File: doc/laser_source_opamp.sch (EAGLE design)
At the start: 12 parts, among them IC1 LM358N

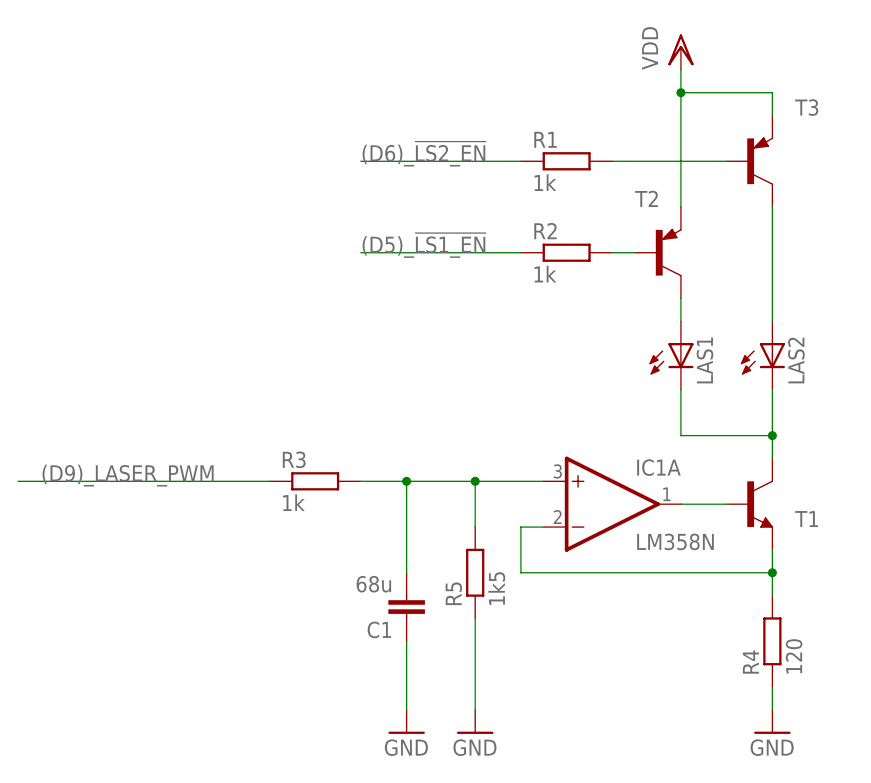
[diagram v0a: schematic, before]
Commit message: Laser power source schematics updated and tested @5V.
The previous version of schematics doesn't work as intended
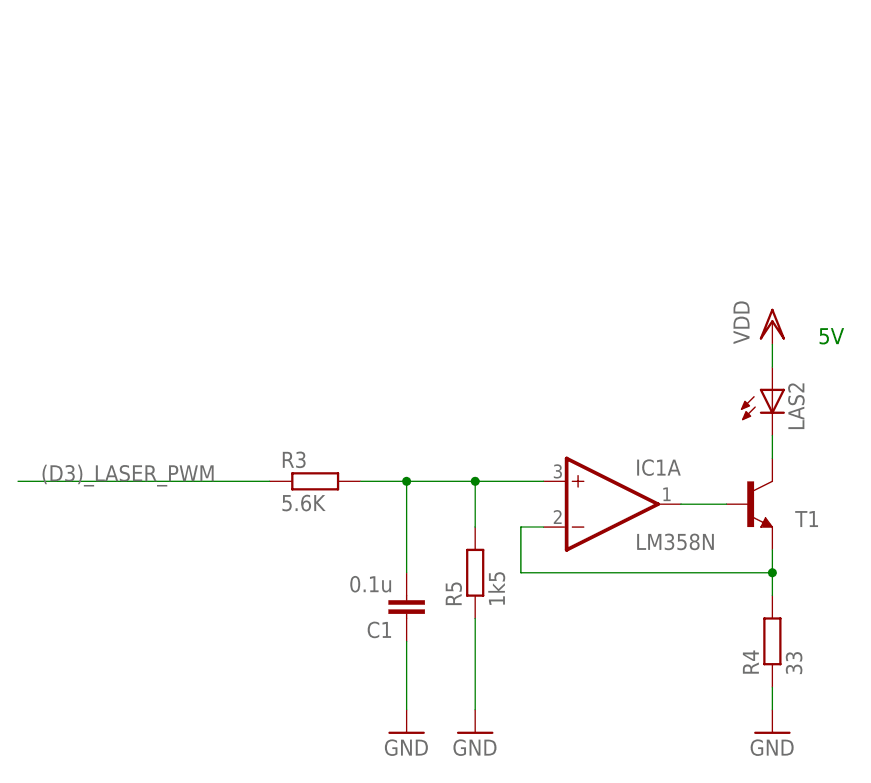
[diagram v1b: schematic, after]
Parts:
- removed LAS1: (no value), led:LED
- removed R1, R2: 1k, rcl:R-EU_0204/5
- removed T2, T3: (no value), transistor:-PNP-SOT23-EBC
- C1: value 68u -> 0.1u
- R3: value 1k -> 5.6K
- R4: value 120 -> 33
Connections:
- net (D9)_LASER_PWM renamed (D3)_LASER_PWM
- removed net (D5)_!LS1_EN!: R2.1
- removed net (D6)_!LS2_EN!: R1.1
- removed net N$10: R2.2, T2.B
- removed net N$7: R1.2, T3.B
- removed net N$8: LAS2.A, T3.C
- removed net N$9: LAS1.A, T2.C
- net N$4: no longer LAS1.C
- net VDD: now also LAS2.A; no longer T2.E, T3.E
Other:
- note added: "5V"
- moved on the sheet: LAS2
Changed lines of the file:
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@@
 </classes>
 <parts>
-<part name="R1" library="rcl" deviceset="R-EU_" device="0204/5" value="1k"/>
-<part name="R2" library="rcl" deviceset="R-EU_" device="0204/5" value="1k"/>
-<part name="R3" library="rcl" deviceset="R-EU_" device="0204/5" value="1k"/>
-<part name="R4" library="rcl" deviceset="R-EU_" device="0204/5" value="120"/>
-<part name="C1" library="capacitor-wima" deviceset="C" device="5/3.5" value="68u"/>
+<part name="R3" library="rcl" deviceset="R-EU_" device="0204/5" value="5.6K"/>
+<part name="R4" library="rcl" deviceset="R-EU_" device="0204/5" value="33"/>
+<part name="C1" library="capacitor-wima" deviceset="C" device="5/3.5" value="0.1u"/>
 <part name="GND1" library="supply1" deviceset="GND" device=""/>
 <part name="VDD1" library="supply1" deviceset="VDD" device=""/>
 <part name="T1" library="transistor" deviceset="*-NPN-" device="SOT89-BCE"/>
-<part name="T2" library="transistor" deviceset="*-PNP-" device="SOT23-EBC"/>
-<part name="T3" library="transistor" deviceset="*-PNP-" device="SOT23-EBC"/>
 <part name="GND2" library="supply1" deviceset="GND" device=""/>
 <part name="LAS2" library="led" deviceset="LED" device=""/>
-<part name="LAS1" library="led" deviceset="LED" device=""/>
 <part name="IC1" library="linear" deviceset="LM358" device="N"/>
 <part name="R5" library="rcl" deviceset="R-EU_" device="0204/5" value="1k5"/>
@@
 <sheet>
 <plain>
+<text x="76.2" y="53.34" size="1.778" layer="91">5V</text>
 </plain>
 <instances>
-<instance part="R1" gate="G$1" x="48.26" y="73.66"/>
-<instance part="R2" gate="G$1" x="48.26" y="63.5"/>
 <instance part="R3" gate="G$1" x="20.32" y="38.1"/>
 <instance part="R4" gate="G$1" x="71.12" y="20.32" rot="R90"/>
 <instance part="C1" gate="G$1" x="30.48" y="22.86" rot="R180"/>
 <instance part="GND1" gate="1" x="71.12" y="10.16"/>
-<instance part="VDD1" gate="G$1" x="60.96" y="86.36"/>
+<instance part="VDD1" gate="G$1" x="71.12" y="55.88"/>
 <instance part="T1" gate="G$1" x="68.58" y="35.56" smashed="yes">
 <attribute name="NAME" x="73.66" y="33.02" size="1.778" layer="95"/>
 <attribute name="VALUE" x="58.42" y="40.64" size="1.778" layer="96"/>
 </instance>
-<instance part="T2" gate="G$1" x="58.42" y="63.5" smashed="yes">
-<attribute name="NAME" x="55.88" y="68.58" size="1.778" layer="95"/>
-<attribute name="VALUE" x="48.26" y="68.58" size="1.778" layer="96"/>
-</instance>
-<instance part="T3" gate="G$1" x="68.58" y="73.66" smashed="yes">
-<attribute name="NAME" x="73.66" y="78.74" size="1.778" layer="95"/>
-<attribute name="VALUE" x="58.42" y="78.74" size="1.778" layer="96"/>
-</instance>
 <instance part="GND2" gate="1" x="30.48" y="10.16"/>
-<instance part="LAS2" gate="G$1" x="71.12" y="53.34"/>
-<instance part="LAS1" gate="G$1" x="60.96" y="53.34"/>
+<instance part="LAS2" gate="G$1" x="71.12" y="48.26"/>
 <instance part="IC1" gate="A" x="53.34" y="35.56"/>
 <instance part="R5" gate="G$1" x="38.1" y="27.94" rot="R90"/>
@@
 </segment>
 </net>
-<net name="(D9)_LASER_PWM" class="0">
+<net name="(D3)_LASER_PWM" class="0">
 <segment>
 <pinref part="R3" gate="G$1" pin="1"/>
@@
 <net name="N$4" class="0">
 <segment>
-<pinref part="LAS1" gate="G$1" pin="C"/>
-<wire x1="60.96" y1="48.26" x2="60.96" y2="43.18" width="0.1524" layer="91"/>
-<wire x1="60.96" y1="43.18" x2="71.12" y2="43.18" width="0.1524" layer="91"/>
 <pinref part="T1" gate="G$1" pin="C"/>
+<pinref part="LAS2" gate="G$1" pin="C"/>
 <wire x1="71.12" y1="43.18" x2="71.12" y2="40.64" width="0.1524" layer="91"/>
-<pinref part="LAS2" gate="G$1" pin="C"/>
-<wire x1="71.12" y1="48.26" x2="71.12" y2="43.18" width="0.1524" layer="91"/>
-<junction x="71.12" y="43.18"/>
-</segment>
-</net>
-<net name="(D5)_!LS1_EN!" class="0">
-<segment>
-<pinref part="R2" gate="G$1" pin="1"/>
-<wire x1="43.18" y1="63.5" x2="25.4" y2="63.5" width="0.1524" layer="91"/>
-<label x="25.4" y="63.5" size="1.778" layer="95"/>
-</segment>
-</net>
-<net name="(D6)_!LS2_EN!" class="0">
-<segment>
-<pinref part="R1" gate="G$1" pin="1"/>
-<wire x1="43.18" y1="73.66" x2="25.4" y2="73.66" width="0.1524" layer="91"/>
-<label x="25.4" y="73.66" size="1.778" layer="95"/>
-</segment>
-</net>
-<net name="N$7" class="0">
-<segment>
-<pinref part="R1" gate="G$1" pin="2"/>
-<pinref part="T3" gate="G$1" pin="B"/>
-<wire x1="53.34" y1="73.66" x2="66.04" y2="73.66" width="0.1524" layer="91"/>
-</segment>
-</net>
-<net name="N$8" class="0">
-<segment>
-<pinref part="T3" gate="G$1" pin="C"/>
-<pinref part="LAS2" gate="G$1" pin="A"/>
-<wire x1="71.12" y1="68.58" x2="71.12" y2="55.88" width="0.1524" layer="91"/>
-</segment>
-</net>
-<net name="N$9" class="0">
-<segment>
-<pinref part="T2" gate="G$1" pin="C"/>
-<pinref part="LAS1" gate="G$1" pin="A"/>
-<wire x1="60.96" y1="58.42" x2="60.96" y2="55.88" width="0.1524" layer="91"/>
-</segment>
-</net>
-<net name="N$10" class="0">
-<segment>
-<pinref part="R2" gate="G$1" pin="2"/>
-<pinref part="T2" gate="G$1" pin="B"/>
-<wire x1="53.34" y1="63.5" x2="55.88" y2="63.5" width="0.1524" layer="91"/>
-</segment>
-</net>
-<net name="VDD" class="0">
-<segment>
-<pinref part="VDD1" gate="G$1" pin="VDD"/>
-<wire x1="60.96" y1="83.82" x2="60.96" y2="81.28" width="0.1524" layer="91"/>
-<wire x1="60.96" y1="81.28" x2="71.12" y2="81.28" width="0.1524" layer="91"/>
-<pinref part="T3" gate="G$1" pin="E"/>
-<wire x1="71.12" y1="81.28" x2="71.12" y2="78.74" width="0.1524" layer="91"/>
-<pinref part="T2" gate="G$1" pin="E"/>
-<wire x1="60.96" y1="81.28" x2="60.96" y2="68.58" width="0.1524" layer="91"/>
-<junction x="60.96" y="81.28"/>
 </segment>
 </net>
@@
 </segment>
 </net>
+<net name="VDD" class="0">
+<segment>
+<pinref part="LAS2" gate="G$1" pin="A"/>
+<wire x1="71.12" y1="53.34" x2="71.12" y2="50.8" width="0.1524" layer="91"/>
+<pinref part="VDD1" gate="G$1" pin="VDD"/>
+</segment>
+</net>
